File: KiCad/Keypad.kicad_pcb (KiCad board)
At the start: 2 copper layers, 19 x 29 mm, 16 parts, among them J1 SPOX, J2 Molex, J3 USB-C, U1 ESP32-WROOM-32, U2 SP3458, U3 FT231XQ

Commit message: Library update
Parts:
- removed Reg1: 3.3V, RevK:RegulatorBlock
- added C2: 0.1uF, RevK:Hidden, F.Cu at (123.2, 114.9)
- added C3: 2.2uF, RevK:Hidden, F.Cu at (126.7, 113.7)
- added C4: 10uF, RevK:Hidden, F.Cu at (126.7, 107.4)
- added D3: Schottky, RevK:Hidden, F.Cu at (126.4, 110.5)
- added L1: 6.8uH, RevK:Hidden, F.Cu at (123.2, 108.9)
- added U4: LMR16006YQ3, RevK:RegulatorBlock, F.Cu at (123.2, 112.8)

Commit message: Kicad 6
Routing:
- net +3V3: track 62.2 -> 63.8 mm
- net Net-(J1-Pad4): track 15.8 -> 14.9 mm
- net Net-(J1-Pad3): track 15.5 -> 14.7 mm
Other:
- net class Default removed
- board text added: "${DATE} Keypad"
- board text removed: "2021-08-05 Keypad"

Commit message: Kicad tidy
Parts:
- turned L1 to 90 degrees

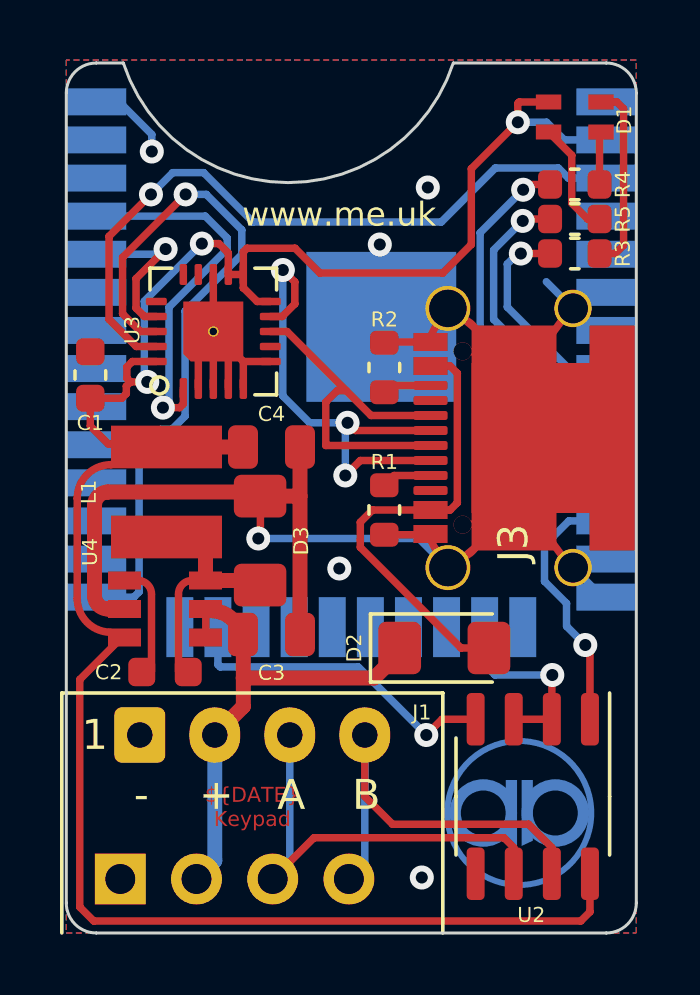
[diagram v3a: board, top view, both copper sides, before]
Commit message: Rework for PSu change
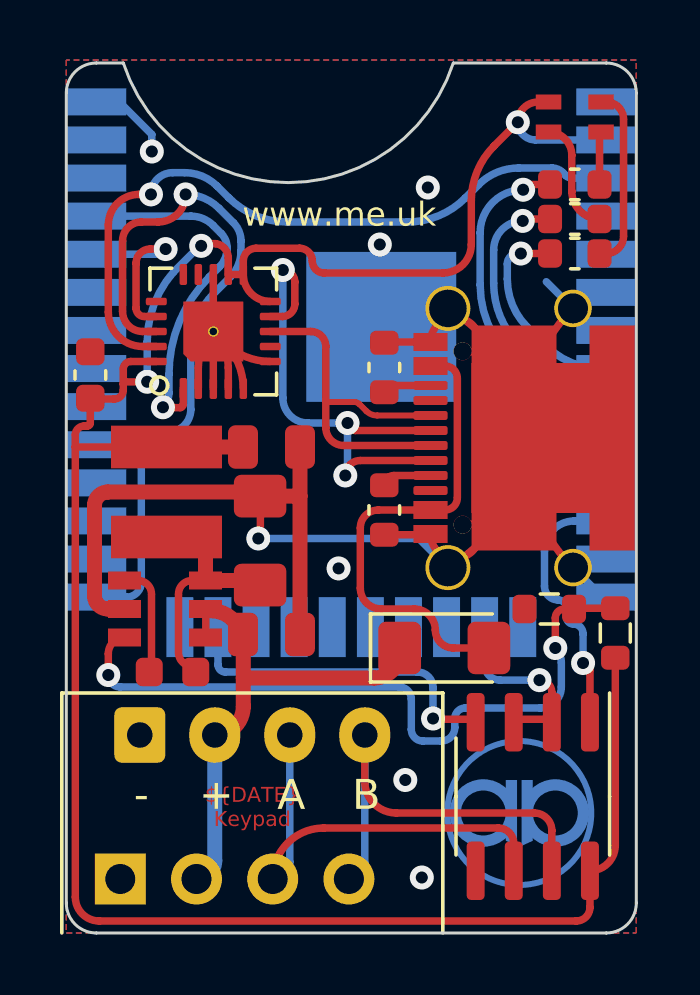
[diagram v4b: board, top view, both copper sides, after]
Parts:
- added R6: 10M 1% or 0R, RevK:R_0603, F.Cu at (138.2, 113.6)
- added R7: 3M 1% or NF, RevK:R_0603, F.Cu at (136.0, 112.8)
- U2: value SP3458 -> SP3485; footprint Package_SO:SO-8_3.9x4.9mm_P1.27mm -> Package_SO:SOIC-8_3.9x4.9mm_P1.27mm
- U4: value LMR16006YQ3 -> LMR16006+FB; footprint RevK:RegulatorBlock -> RevK:RegulatorBlockFB
- moved C2 0.25 mm to (123.4, 114.9)
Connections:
- J3 pad A8: Net-(J3-PadA8) -> unconnected-(J3-PadA8)
- J3 pad B8: Net-(J3-PadB8) -> unconnected-(J3-PadB8)
- U1 pad 10: Net-(U1-Pad10) -> unconnected-(U1-Pad10)
- U1 pad 17: Net-(U1-Pad17) -> unconnected-(U1-Pad17)
- U1 pad 18: Net-(U1-Pad18) -> unconnected-(U1-Pad18)
- U1 pad 19: Net-(U1-Pad19) -> unconnected-(U1-Pad19)
- U1 pad 20: Net-(U1-Pad20) -> unconnected-(U1-Pad20)
- U1 pad 21: Net-(U1-Pad21) -> unconnected-(U1-Pad21)
- U1 pad 22: Net-(U1-Pad22) -> unconnected-(U1-Pad22)
- U1 pad 24: Net-(U1-Pad24) -> unconnected-(U1-Pad24)
- U1 pad 26: Net-(U1-Pad26) -> unconnected-(U1-Pad26)
- U1 pad 27: Net-(U1-Pad27) -> unconnected-(U1-Pad27)
- U1 pad 28: Net-(U1-Pad28) -> unconnected-(U1-Pad28)
- U1 pad 29: Net-(U1-Pad29) -> unconnected-(U1-Pad29)
- U1 pad 30: Net-(U1-Pad30) -> unconnected-(U1-Pad30)
- U1 pad 31: Net-(U1-Pad31) -> unconnected-(U1-Pad31)
- U1 pad 32: Net-(U1-Pad32) -> unconnected-(U1-Pad32)
- U1 pad 33: Net-(U1-Pad33) -> unconnected-(U1-Pad33)
- U1 pad 36: Net-(U1-Pad36) -> unconnected-(U1-Pad36)
- U1 pad 37: Net-(U1-Pad37) -> unconnected-(U1-Pad37)
- U1 pad 4: Net-(U1-Pad4) -> unconnected-(U1-Pad4)
- U1 pad 5: Net-(U1-Pad5) -> unconnected-(U1-Pad5)
- U3 pad 14: Net-(U3-Pad14) -> unconnected-(U3-Pad14)
- U3 pad 15: Net-(U3-Pad15) -> unconnected-(U3-Pad15)
- U3 pad 16: Net-(U3-Pad16) -> unconnected-(U3-Pad16)
- U3 pad 7: Net-(U3-Pad7) -> unconnected-(U3-Pad7)
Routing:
- net Net-(R6-Pad2): track 0.00 -> 23.9 mm, vias 0 -> 2
- net +3V3: track 63.8 -> 77.8 mm
- net VBUS: track 15.3 -> 16.2 mm
- net Net-(J1-Pad3): track 14.7 -> 15.2 mm
- net GND: track 32.2 -> 32.7 mm, vias 6 -> 7

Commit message: Tweak
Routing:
- net DE: track 6.24 -> 7.09 mm
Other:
- board text added: "${DATE}"

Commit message: Updated for VBUS and GPIO changes
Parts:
- moved Logo1 2.40 mm to (135.0, 119.6)

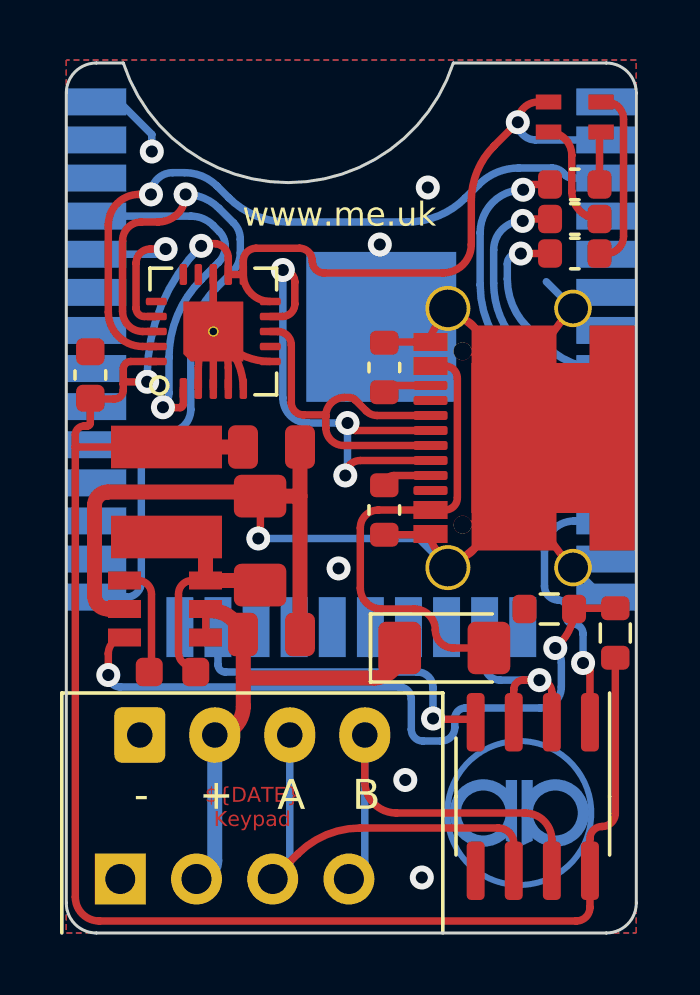
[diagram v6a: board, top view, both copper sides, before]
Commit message: VBUS update
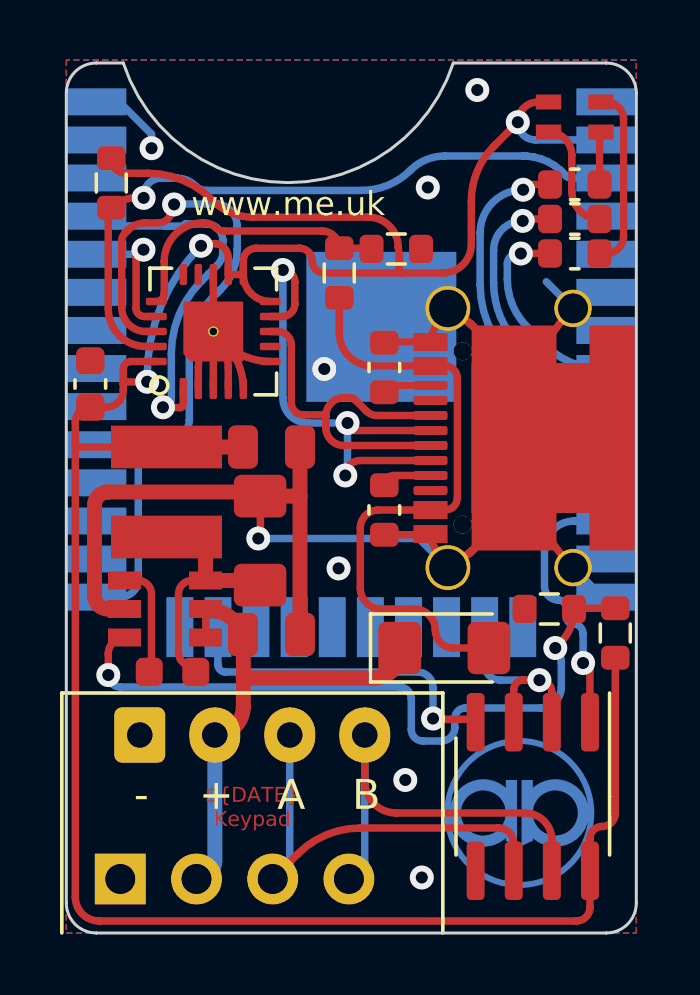
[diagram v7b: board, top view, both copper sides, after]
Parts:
- added R1: 10k, RevK:R_0603, F.Cu at (121.4, 98.6)
- added R4: 4k7, RevK:R_0603, F.Cu at (129.0, 101.6)
- added R5: 10k, RevK:R_0603, F.Cu at (130.9, 100.8)
- moved C1 0.30 mm to (120.7, 105.3)
- renumbered R7 to R10, R1 to R2, R2 to R3, R3 to R6, R4 to R7, R5 to R8, R6 to R9
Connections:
- U3 pad 16: unconnected-(U3-Pad16) -> Net-(R4-Pad2)
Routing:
- net +3V3: track 77.7 -> 89.1 mm
- net Net-(R4-Pad2): track 0.00 -> 9.45 mm
- net VBUS: track 16.2 -> 21.0 mm
- net I: track 5.94 -> 4.68 mm
- net GND: track 32.7 -> 32.6 mm, vias 7 -> 8

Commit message: Resistor fixes
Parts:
- R10: value 3M 1% or NF -> 30k 1% or NF
- R9: value 10M 1% or 0R -> 100k 1% or 0R
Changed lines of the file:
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@@
       (effects (font (size 0.5 0.5) (thickness 0.08)))
     )
-    (fp_text value "3M 1% or NF" (at 0 0) (layer "F.Fab")
+    (fp_text value "30k 1% or NF" (at 0 0) (layer "F.Fab")
       (effects (font (size 0.4 0.4) (thickness 0.08)))
     )
@@
       (effects (font (size 0.5 0.5) (thickness 0.08)))
     )
-    (fp_text value "10M 1% or 0R" (at 0 0 90) (layer "F.Fab")
-      (effects (font (size 0.4 0.4) (thickness 0.08)))
-    )
+    (fp_text value "100k 1% or 0R" (at 0 0 90) (layer "F.Fab")
+      (effects (font (size 0.4 0.4) (thickness 0.08)))
+    )
